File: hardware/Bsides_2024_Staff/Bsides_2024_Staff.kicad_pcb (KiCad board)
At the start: 2 copper layers, 129.4 x 129.4 mm, 45 parts, among them J1 Serial_IN, J2 Add_On, J3 OLED, J4 Serial_OUT, J5 Battery, J6 Battery, P1 USB_C_Plug_USB2.0, Q1 DMG3415U-7, SW1 ON, SW2 RESET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

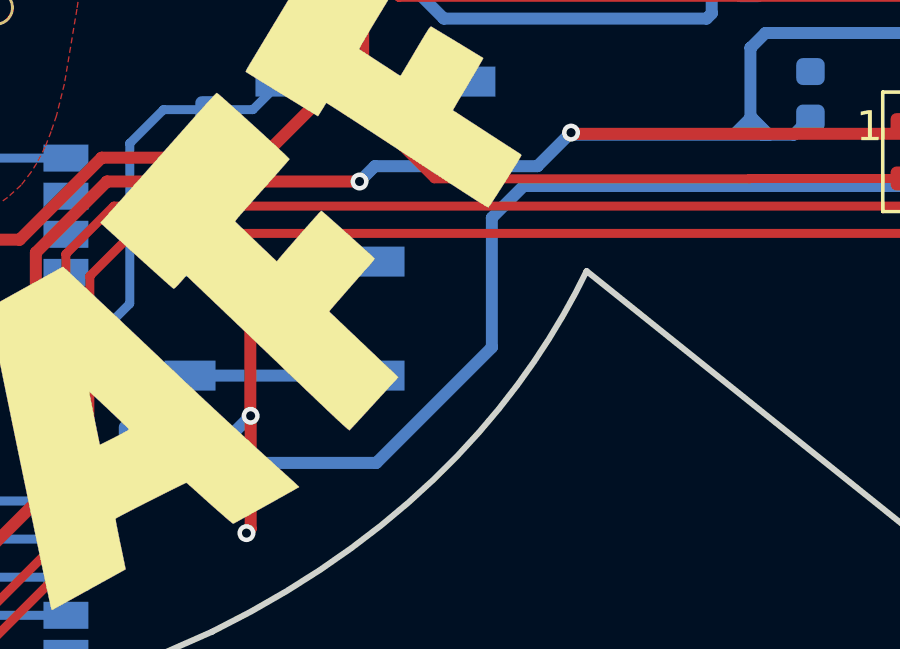
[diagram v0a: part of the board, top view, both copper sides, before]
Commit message: fet(Hw): Update route
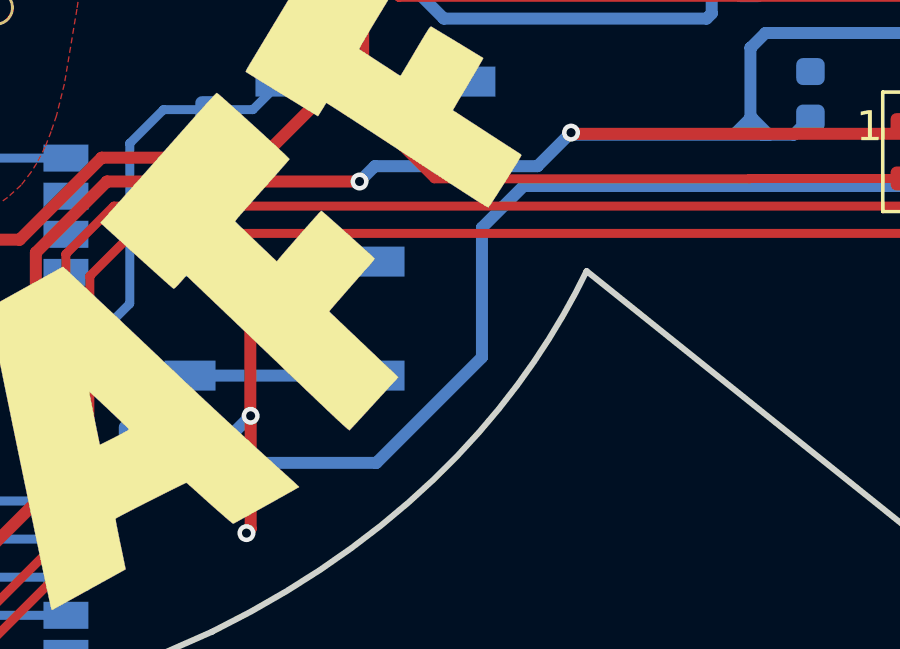
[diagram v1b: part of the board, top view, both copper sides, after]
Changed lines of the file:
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@@
+	)
+	(segment
+		(start 192.075 132.02)
+		(end 174.45 132.02)
+		(width 0.4)
+		(layer "B.Cu")
+		(net 16)
+	)
+	(segment
+		(start 173.06 137.73)
+		(end 169.54 141.25)
+		(width 0.4)
+		(layer "B.Cu")
+		(net 16)
 	)
 	(segment
@@
 	)
 	(segment
-		(start 173.39 133.08)
-		(end 173.39 137.4)
+		(start 174.45 132.02)
+		(end 173.06 133.41)
 		(width 0.4)
 		(layer "B.Cu")
@@
 	)
 	(segment
-		(start 174.45 132.02)
-		(end 173.39 133.08)
-		(width 0.4)
-		(layer "B.Cu")
-		(net 16)
-	)
-	(segment
-		(start 173.39 137.4)
-		(end 169.54 141.25)
+		(start 192.47 130.16)
+		(end 192.47 131.625)
 		(width 0.4)
 		(layer "B.Cu")
@@
 	)
 	(segment
-		(start 192.47 130.16)
-		(end 192.47 131.625)
+		(start 173.06 133.41)
+		(end 173.06 137.73)
 		(width 0.4)
 		(layer "B.Cu")
-		(net 16)
-	)
-	(segment
-		(start 192.075 132.02)
-		(end 174.45 132.02)
-		(width 0.4)
-		(layer "B.Cu")

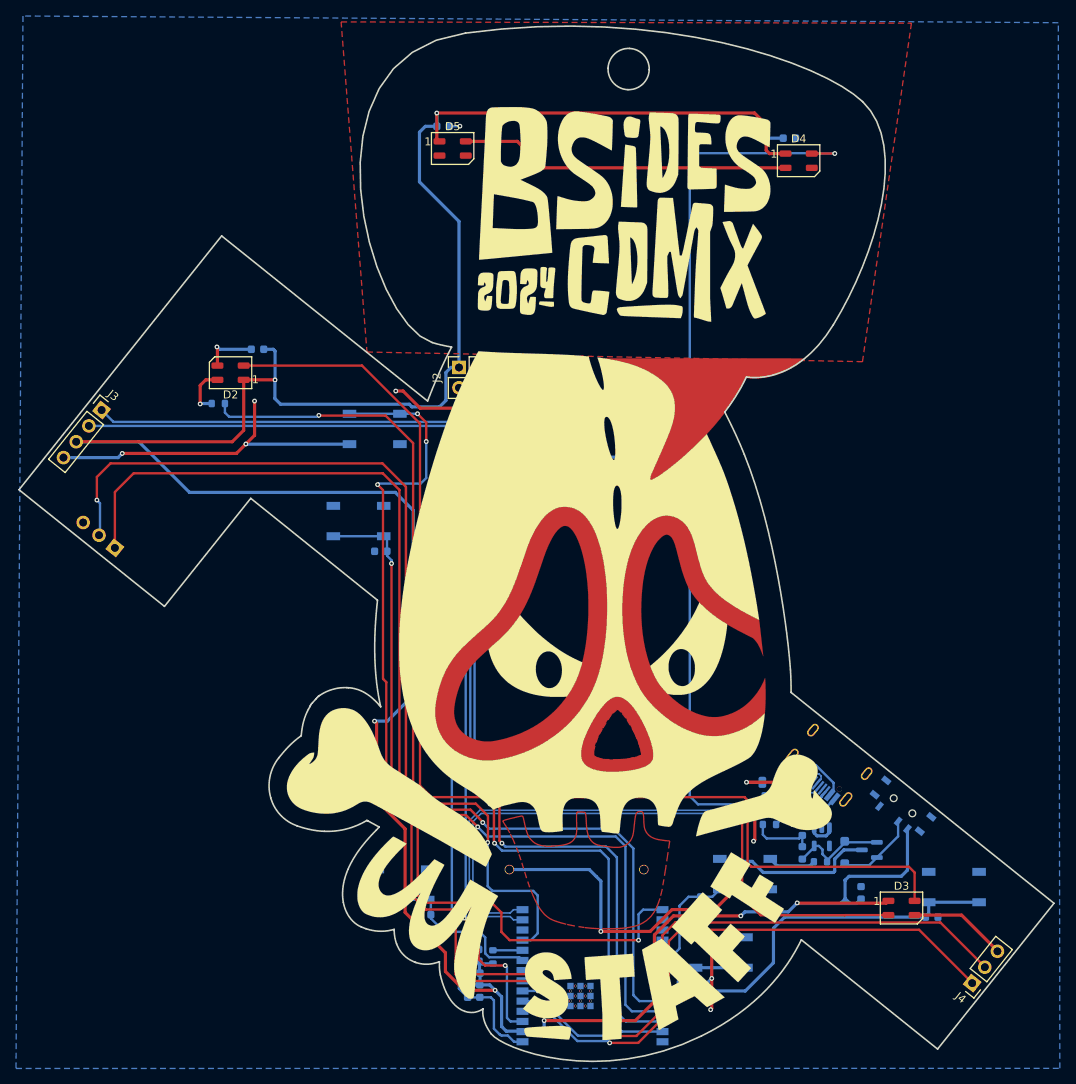
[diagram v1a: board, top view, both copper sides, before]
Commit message: feat(Hw):Moved_Buttons_Speaker
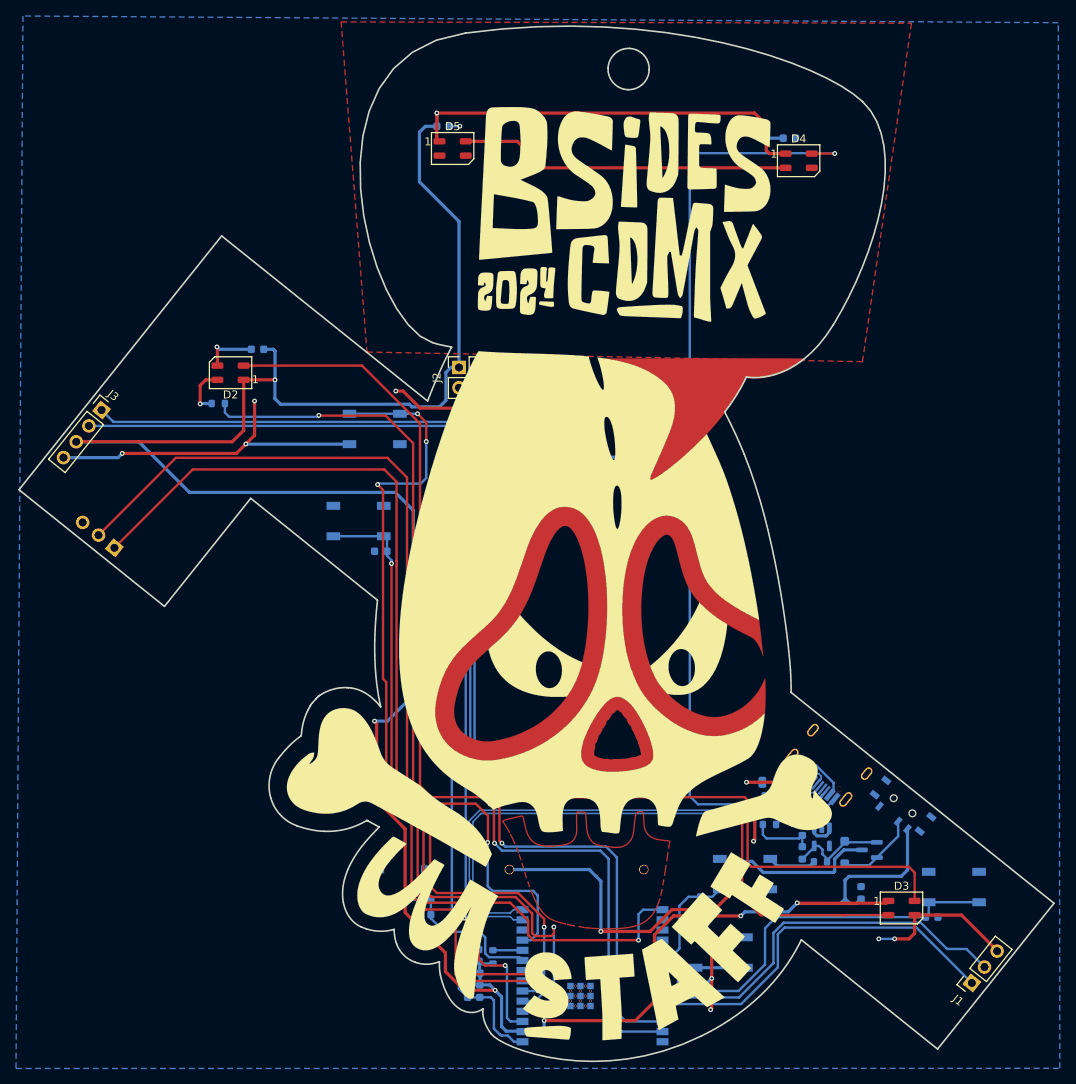
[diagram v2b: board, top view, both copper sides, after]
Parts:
- J1: moved to F.Cu
- J4: moved to B.Cu
- moved J4 120.2 mm to (90.7, 85.9), turned to 51.3 degrees
- moved J1 120.1 mm to (197.9, 140.3), turned to 141.6 degrees
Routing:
- net /GPIO17: track 139.8 -> 48.8 mm, vias 2 -> 0
- net /GPIO16: track 138.2 -> 48.3 mm, vias 1 -> 0
- net /GPIO4: track 71.7 -> 127.3 mm
- net /GPIO5: track 73.5 -> 124.1 mm
- net GND: track 134.6 -> 143.8 mm, vias 12 -> 14

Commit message: feat(Hw): Labels added
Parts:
- added kibuzzard-666B5A62: G***, kibuzzard-666B5A62, F.Cu at (195.4, 138.7)
- added kibuzzard-666B5A62: G***, kibuzzard-666B5A62, B.Cu at (90.6, 82.0)
- added kibuzzard-666B5A91: G***, kibuzzard-666B5A91, F.Cu at (197.1, 136.6)
- added kibuzzard-666B5A91: G***, kibuzzard-666B5A91, B.Cu at (92.5, 83.6)
- added kibuzzard-666B5AA1: G***, kibuzzard-666B5AA1, F.Cu at (198.6, 134.1)
- added kibuzzard-666B5AA1: G***, kibuzzard-666B5AA1, B.Cu at (88.7, 80.1)
- added kibuzzard-666B5BCA: G***, kibuzzard-666B5BCA, B.Cu at (133.9, 68.7)
- added kibuzzard-666B5C0A: G***, kibuzzard-666B5C0A, B.Cu at (133.8, 61.0)
- added kibuzzard-666B5C24: G***, kibuzzard-666B5C24, B.Cu at (136.4, 68.8)
- added kibuzzard-666B5C33: G***, kibuzzard-666B5C33, B.Cu at (136.5, 60.2)
- F1: value 0.5A -> 0.75A
- moved J6 0.12 mm to (157.0, 100.3)

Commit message: feat(Hw): Update labels
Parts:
- added kibuzzard-666B5BCA: G***, kibuzzard-666B5BCA, B.Cu at (140.0, 124.2)
- added kibuzzard-666B5BCA: G***, kibuzzard-666B5BCA, B.Cu at (157.0, 76.7)
- added kibuzzard-666B5C0A: G***, kibuzzard-666B5C0A, B.Cu at (140.1, 76.2)
- added kibuzzard-666B5C0A: G***, kibuzzard-666B5C0A, B.Cu at (156.9, 124.1)

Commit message: feat(Hw): Update labels
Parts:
- removed the kibuzzard-666B5BCA at (157.0, 76.7)
- removed the kibuzzard-666B5C0A at (140.1, 76.2)
- moved kibuzzard-666B5C0A 6.47 mm to (161.1, 129.1)
- moved kibuzzard-666B5BCA 5.32 mm to (138.4, 129.3)
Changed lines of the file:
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@@
 	(footprint "kibuzzard-666B5BCA"
 		(layer "B.Cu")
-		(at 140.01 124.21 180)
+		(at 138.42 129.29 180)
 		(descr "Generated with KiBuzzard")
 		(tags "kb_params=eyJBbGlnbm1lbnRDaG9pY2UiOiAiQ2VudGVyIiwgIkNhcExlZnRDaG9pY2UiOiAiWyIsICJDYXBSaWdodENob2ljZSI6ICJdIiwgIkZvbnRDb21ib0JveCI6ICJVYnVudHVNb25vLUIiLCAiSGVpZ2h0Q3RybCI6IDEuMCwgIkxheWVyQ29tYm9Cb3giOiAiRi5TaWxrUyIsICJMaW5lU3BhY2luZ0N0cmwiOiAxLjUsICJNdWx0aUxpbmVUZXh0IjogIisiLCAiUGFkZGluZ0JvdHRvbUN0cmwiOiAxLjAsICJQYWRkaW5nTGVmdEN0cmwiOiAyLjUsICJQYWRkaW5nUmlnaHRDdHJsIjogMi41LCAiUGFkZGluZ1RvcEN0cmwiOiAxLjAsICJXaWR0aEN0cmwiOiAxLjB9")
 		(property "Reference" "kibuzzard-666B5BCA"
-			(at 0 3.733598 360)
+			(at 0 3.733598 0)
 			(layer "B.SilkS")
 			(hide yes)
@@
 		)
 		(property "Value" "G***"
-			(at 0 -3.733598 360)
+			(at 0 -3.733598 0)
 			(layer "B.SilkS")
 			(hide yes)
@@
 		)
 		(property "Footprint" ""
-			(at 0 0 360)
+			(at 0 0 0)
 			(layer "B.Fab")
 			(hide yes)
@@
 		)
 		(property "Datasheet" ""
-			(at 0 0 360)
+			(at 0 0 0)
 			(layer "B.Fab")
 			(hide yes)
@@
 		)
 		(property "Description" ""
-			(at 0 0 360)
+			(at 0 0 0)
 			(layer "B.Fab")
 			(hide yes)
@@
 	(footprint "kibuzzard-666B5C0A"
 		(layer "B.Cu")
-		(at 140.09 76.24 180)
+		(at 161.05 129.1)
 		(descr "Generated with KiBuzzard")
 		(tags "kb_params=eyJBbGlnbm1lbnRDaG9pY2UiOiAiQ2VudGVyIiwgIkNhcExlZnRDaG9pY2UiOiAiWyIsICJDYXBSaWdodENob2ljZSI6ICJdIiwgIkZvbnRDb21ib0JveCI6ICJVYnVudHVNb25vLUIiLCAiSGVpZ2h0Q3RybCI6IDAuMiwgIkxheWVyQ29tYm9Cb3giOiAiRi5TaWxrUyIsICJMaW5lU3BhY2luZ0N0cmwiOiAyLjAsICJNdWx0aUxpbmVUZXh0IjogIi0iLCAiUGFkZGluZ0JvdHRvbUN0cmwiOiAyLjAsICJQYWRkaW5nTGVmdEN0cmwiOiAyLjAsICJQYWRkaW5nUmlnaHRDdHJsIjogMi4wLCAiUGFkZGluZ1RvcEN0cmwiOiAyLjAsICJXaWR0aEN0cmwiOiAwLjZ9")
@@
 		(property "Description" ""
 			(at 0 0 0)
-			(layer "B.Fab")
-			(hide yes)
-			(effects
-				(font
-					(size 1.27 1.27)
-					(thickness 0.15)
-				)
-				(justify mirror)
-			)
-		)
-		(attr board_only exclude_from_pos_files exclude_from_bom)
-		(fp_poly
-			(pts
-				(xy -0.226446 0.375482) (xy -0.501928 0.375482) (xy -0.501928 -0.375482) (xy -0.226446 -0.375482)
-				(xy 0.226446 -0.375482) (xy 0.226446 -0.1) (xy -0.226446 -0.1) (xy -0.226446 0.1) (xy 0.226446 0.1)
-				(xy 0.226446 -0.1) (xy 0.226446 -0.375482) (xy 0.501928 -0.375482) (xy 0.501928 0.375482) (xy 0.226446 0.375482)
-				(xy -0.226446 0.375482)
-			)
-			(stroke
-				(width 0)
-				(type solid)
-			)
-			(fill solid)
-			(layer "B.SilkS")
-		)
-	)
-	(footprint "kibuzzard-666B5C0A"
-		(layer "B.Cu")
-		(at 156.95 124.09)
-		(descr "Generated with KiBuzzard")
-		(tags "kb_params=eyJBbGlnbm1lbnRDaG9pY2UiOiAiQ2VudGVyIiwgIkNhcExlZnRDaG9pY2UiOiAiWyIsICJDYXBSaWdodENob2ljZSI6ICJdIiwgIkZvbnRDb21ib0JveCI6ICJVYnVudHVNb25vLUIiLCAiSGVpZ2h0Q3RybCI6IDAuMiwgIkxheWVyQ29tYm9Cb3giOiAiRi5TaWxrUyIsICJMaW5lU3BhY2luZ0N0cmwiOiAyLjAsICJNdWx0aUxpbmVUZXh0IjogIi0iLCAiUGFkZGluZ0JvdHRvbUN0cmwiOiAyLjAsICJQYWRkaW5nTGVmdEN0cmwiOiAyLjAsICJQYWRkaW5nUmlnaHRDdHJsIjogMi4wLCAiUGFkZGluZ1RvcEN0cmwiOiAyLjAsICJXaWR0aEN0cmwiOiAwLjZ9")
-		(property "Reference" "kibuzzard-666B5C0A"
-			(at 0 3.423482 360)
-			(layer "B.SilkS")
-			(hide yes)
-			(effects
-				(font
-					(size 0.001 0.001)
-					(thickness 0.15)
-				)
-				(justify mirror)
-			)
-		)
-		(property "Value" "G***"
-			(at 0 -3.423482 360)
-			(layer "B.SilkS")
-			(hide yes)
-			(effects
-				(font
-					(size 0.001 0.001)
-					(thickness 0.15)
-				)
-				(justify mirror)
-			)
-		)
-		(property "Footprint" ""
-			(at 0 0 360)
-			(layer "B.Fab")
-			(hide yes)
-			(effects
-				(font
-					(size 1.27 1.27)
-					(thickness 0.15)
-				)
-				(justify mirror)
-			)
-		)
-		(property "Datasheet" ""
-			(at 0 0 360)
-			(layer "B.Fab")
-			(hide yes)
-			(effects
-				(font
-					(size 1.27 1.27)
-					(thickness 0.15)
-				)
-				(justify mirror)
-			)
-		)
-		(property "Description" ""
-			(at 0 0 360)
 			(layer "B.Fab")
 			(hide yes)
@@
 			)
 			(stroke
-				(width 0)
-				(type solid)
-			)
-			(fill solid)
-			(layer "B.SilkS")
-		)
-	)
-	(footprint "kibuzzard-666B5BCA"
-		(layer "B.Cu")
-		(at 156.99 76.66)
-		(descr "Generated with KiBuzzard")
-		(tags "kb_params=eyJBbGlnbm1lbnRDaG9pY2UiOiAiQ2VudGVyIiwgIkNhcExlZnRDaG9pY2UiOiAiWyIsICJDYXBSaWdodENob2ljZSI6ICJdIiwgIkZvbnRDb21ib0JveCI6ICJVYnVudHVNb25vLUIiLCAiSGVpZ2h0Q3RybCI6IDEuMCwgIkxheWVyQ29tYm9Cb3giOiAiRi5TaWxrUyIsICJMaW5lU3BhY2luZ0N0cmwiOiAxLjUsICJNdWx0aUxpbmVUZXh0IjogIisiLCAiUGFkZGluZ0JvdHRvbUN0cmwiOiAxLjAsICJQYWRkaW5nTGVmdEN0cmwiOiAyLjUsICJQYWRkaW5nUmlnaHRDdHJsIjogMi41LCAiUGFkZGluZ1RvcEN0cmwiOiAxLjAsICJXaWR0aEN0cmwiOiAxLjB9")
-		(property "Reference" "kibuzzard-666B5BCA"
-			(at 0 3.733598 0)
-			(layer "B.SilkS")
-			(hide yes)
-			(effects
-				(font
-					(size 0.001 0.001)
-					(thickness 0.15)
-				)
-				(justify mirror)
-			)
-		)
-		(property "Value" "G***"
-			(at 0 -3.733598 0)
-			(layer "B.SilkS")
-			(hide yes)
-			(effects
-				(font
-					(size 0.001 0.001)
-					(thickness 0.15)
-				)
-				(justify mirror)
-			)
-		)
-		(property "Footprint" ""
-			(at 0 0 0)
-			(layer "B.Fab")
-			(hide yes)
-			(effects
-				(font
-					(size 1.27 1.27)
-					(thickness 0.15)
-				)
-				(justify mirror)
-			)
-		)
-		(property "Datasheet" ""
-			(at 0 0 0)
-			(layer "B.Fab")
-			(hide yes)
-			(effects
-				(font
-					(size 1.27 1.27)
-					(thickness 0.15)
-				)
-				(justify mirror)
-			)
-		)
-		(property "Description" ""
-			(at 0 0 0)
-			(layer "B.Fab")
-			(hide yes)
-			(effects
-				(font
-					(size 1.27 1.27)
-					(thickness 0.15)
-				)
-				(justify mirror)
-			)
-		)
-		(attr board_only exclude_from_pos_files exclude_from_bom)
-		(fp_poly
-			(pts
-				(xy -0.467706 0.685598) (xy -0.9317 0.685598) (xy -0.9317 -0.685598) (xy -0.467706 -0.685598) (xy 0.11804 -0.685598)
-				(xy 0.11804 -0.5) (xy -0.11804 -0.5) (xy -0.11804 -0.112472) (xy -0.467706 -0.112472) (xy -0.467706 0.112472)
-				(xy -0.11804 0.112472) (xy -0.11804 0.5) (xy 0.11804 0.5) (xy 0.11804 0.112472) (xy 0.467706 0.112472)
-				(xy 0.467706 -0.112472) (xy 0.11804 -0.112472) (xy 0.11804 -0.5) (xy 0.11804 -0.685598) (xy 0.467706 -0.685598)
-				(xy 0.9317 -0.685598) (xy 0.9317 0.685598) (xy 0.467706 0.685598) (xy -0.467706 0.685598)
-			)
-			(stroke

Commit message: feat(Hw): Update schematic and route
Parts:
- added kibuzzard-666C7661: G***, kibuzzard-666C7661, B.Cu at (190.3, 124.2)
- added kibuzzard-666C76B6: G***, kibuzzard-666C76B6, B.Cu at (183.6, 119.2)
- moved P1 0.58 mm to (178.4, 115.0)
- moved J5 0.24 mm to (139.8, 100.3)
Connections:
- net /GPIO1 renamed /LEFT
- net /GPIO15 renamed /RIGHT
- net /GPIO16 renamed /TX
- net /GPIO17 renamed /RX
- net /GPIO22 renamed /UP
- net /GPIO23 renamed /DOWN
- net /GPIO4 renamed /RX1
- net /GPIO5 renamed /TX1
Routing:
- net GND: track 143.8 -> 137.3 mm, vias 14 -> 13
- net /D-: track 66.7 -> 65.1 mm
- net /VOUT: track 373.7 -> 372.6 mm
- net Net-(P1-VCONN): track 8.17 -> 7.37 mm
- net Net-(P1-CC): track 4.64 -> 4.10 mm
